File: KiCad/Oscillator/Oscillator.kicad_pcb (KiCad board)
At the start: 2 copper layers, 78 x 73.5 mm, 51 parts, among them J1 Screw_Terminal_01x02, J2 Screw_Terminal_01x03, Q1 NPN, Q2 PNP, Q3 NPN, Q4 PNP, U1 40106, U2 TL074

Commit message: added silkscreen to help assembly process on all boards
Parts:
- moved RV1 4.34 mm to (64.5, 64.0), turned to 90 degrees
- moved RV6 3.00 mm to (98.5, 64.0), turned to 90 degrees
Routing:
- net -9V: track 165.8 -> 153.7 mm
- net Net-(R5-Pad1): track 7.35 -> 10.6 mm
- net Net-(R1-Pad1): track 7.38 -> 10.6 mm
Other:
- board text added: "Fine Tune 1"
- board text added: "Fine Tune 2"
- board text added: "Mixer"

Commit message: ran DRC on all boards
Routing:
- net GND: track 8.05 -> 10.4 mm, vias 4 -> 5
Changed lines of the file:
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@@
+	)
+	(segment
+		(start 86.65 72.25)
+		(end 85.5 73.4)
+		(width 0.5)
+		(layer "F.Cu")
+		(net "GND")
+	)
+	(segment
+		(start 86.65 71.5)
+		(end 86.65 72.25)
+		(width 0.5)
+		(layer "F.Cu")
+		(net "GND")
 	)
 	(segment
@@
 		(net "GND")
 	)
+	(via
+		(at 85.5 73.4)
+		(size 1.2)
+		(drill 0.7)
+		(layers "F.Cu" "B.Cu")
+		(net "GND")
+	)

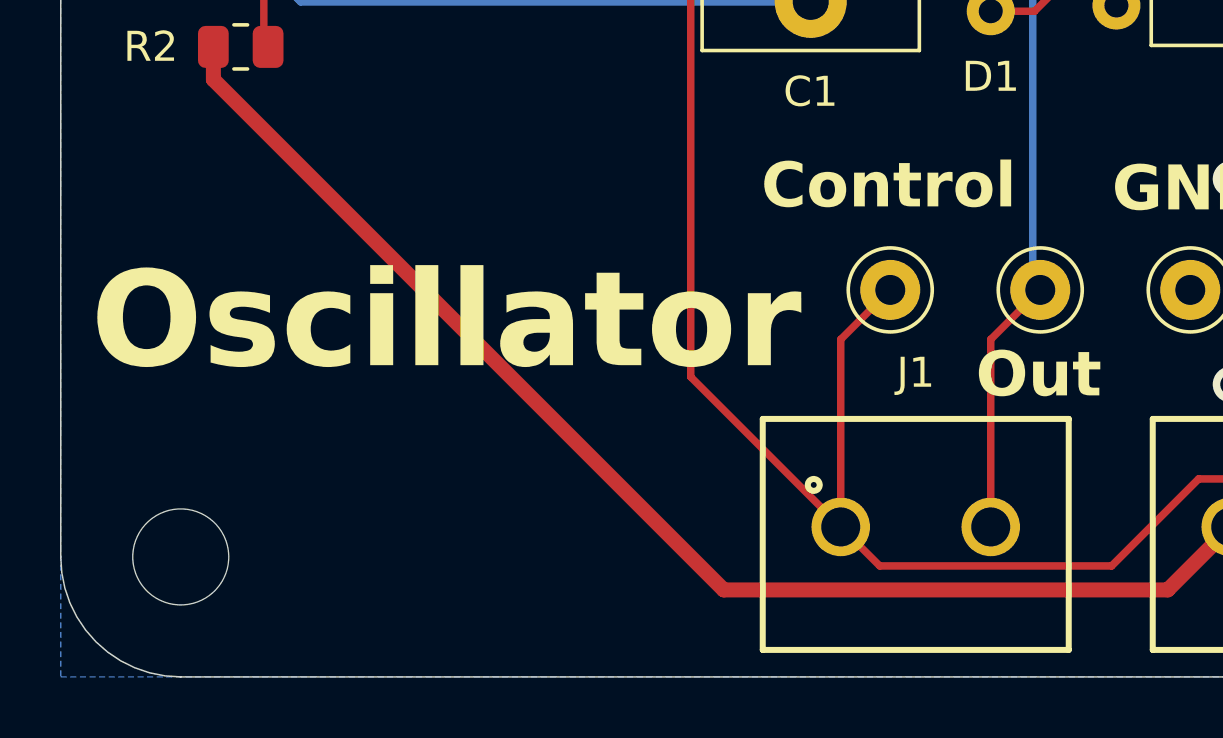
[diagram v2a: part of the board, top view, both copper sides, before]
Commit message: added graphics to some boards
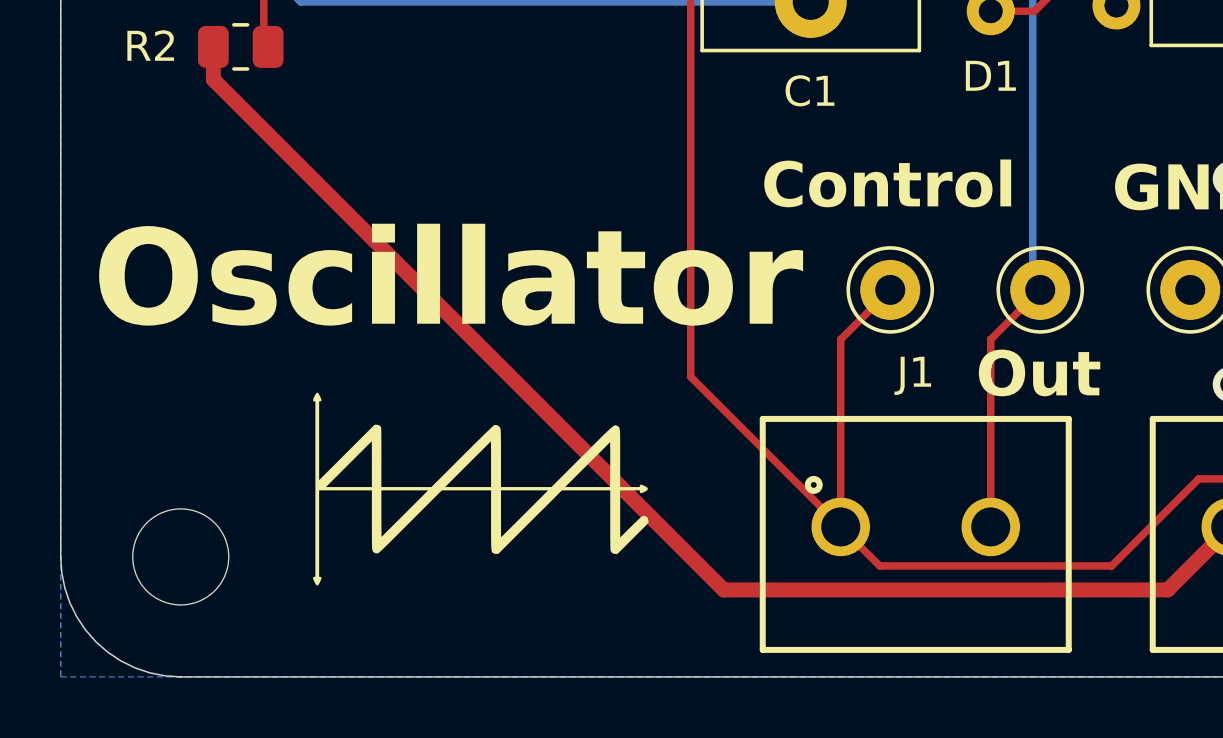
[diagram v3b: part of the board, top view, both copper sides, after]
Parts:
- added G***: LOGO, LOGO, F.Cu at (55.5, 102.6)
